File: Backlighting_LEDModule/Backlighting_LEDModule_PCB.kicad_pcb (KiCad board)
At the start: 2 copper layers, 32.2 x 55 mm, 6 parts, among them J1 Conn_02x10_Odd_Even, J11 BOARD_CONN, J2 Conn_02x10_Odd_Even

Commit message: Fix the swapped EFIS filenames and rename the backlight nets to +5V
Two naming defects, no electrical change on any board.

EFIS sheets
-----------
The root sheet pointed EFIS_LEFT at efis_right.kicad_sch and EFIS_RIGHT at
efis_left.kicad_sch. The schematic was correct, since the file behind the
LEFT sheet did hold the L_* signals, but the filenames said the opposite and
anyone reading the files from outside KiCad would have been misled.

The two files are swapped and every reference follows: the sheet properties
in the root schematic and the 49 sheetfile entries the footprints carry on
the board. Each file now matches the sheet that loads it.

  netlist   198 nets, 135 components, not one node moved
  ERC       0 violations
  DRC       6 violations, all cosmetic, 0 unconnected, 0 parity issues

Backlight nets
--------------
Every net in the backlighting chain was called +9V while carrying 5 V, on
all four boards. The white LEDs sit behind 91 Ω: at 5 V that is 21 mA, right
at the rating for a 1206 white LED, while 9 V would put them at 65 mA. The
name was a leftover from an earlier design and was the kind of label that
eventually makes someone connect the wrong supply.

Renamed across Korry_Large, Korry_Small, Backlighting_Dimmer and
Backlighting_LEDModule, in both the schematics and the boards: the power
symbol, its value, which is what actually names the net, and the net entries
on the copper. 88 occurrences. None of those boards had a +5V net already,
so nothing was merged.

Verified against the state committed a moment ago: ERC and DRC counts are
identical on all four boards, before and after, and no board gained or lost
a connection.

The Readme drops these two entries and gains the defects that surfaced while
checking: the Backlighting_Dimmer footprints carry their reference in the
value field instead of the schematic value, so a BOM read from that board is
wrong; its terminal block footprint no longer exists in the KiCad library;
four texts on the Korry_Large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
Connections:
- net +9V renamed +5V
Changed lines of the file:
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@@
 	(net 0 "")
 	(net 1 "GND")
-	(net 2 "+9V")
+	(net 2 "+5V")
 	(footprint "Connector_PinHeader_2.54mm:PinHeader_2x10_P2.54mm_Vertical"
 		(layer "F.Cu")
@@
 			(layers "*.Cu" "*.Mask")
 			(remove_unused_layers no)
-			(net 2 "+9V")
+			(net 2 "+5V")
 			(pinfunction "Pin_2")
 			(pintype "passive")
@@
 			(layers "*.Cu" "*.Mask")
 			(remove_unused_layers no)
-			(net 2 "+9V")
+			(net 2 "+5V")
 			(pinfunction "Pin_4")
 			(pintype "passive")
@@
 			(layers "*.Cu" "*.Mask")
 			(remove_unused_layers no)
-			(net 2 "+9V")
+			(net 2 "+5V")
 			(pinfunction "Pin_6")
 			(pintype "passive")
@@
 			(layers "*.Cu" "*.Mask")
 			(remove_unused_layers no)
-			(net 2 "+9V")
+			(net 2 "+5V")
 			(pinfunction "Pin_8")
 			(pintype "passive")
@@
 			(layers "*.Cu" "*.Mask")
 			(remove_unused_layers no)
-			(net 2 "+9V")
+			(net 2 "+5V")
 			(pinfunction "Pin_10")
 			(pintype "passive")
@@
 			(layers "*.Cu" "*.Mask")
 			(remove_unused_layers no)
-			(net 2 "+9V")
+			(net 2 "+5V")
 			(pinfunction "Pin_12")
 			(pintype "passive")
@@
 			(layers "*.Cu" "*.Mask")
 			(remove_unused_layers no)
-			(net 2 "+9V")
+			(net 2 "+5V")
 			(pinfunction "Pin_14")
 			(pintype "passive")
@@
 			(layers "*.Cu" "*.Mask")
 			(remove_unused_layers no)
-			(net 2 "+9V")
+			(net 2 "+5V")
 			(pinfunction "Pin_16")
 			(pintype "passive")
@@
 			(layers "*.Cu" "*.Mask")
 			(remove_unused_layers no)
-			(net 2 "+9V")
+			(net 2 "+5V")
 			(pinfunction "Pin_18")
 			(pintype "passive")
@@
 			(layers "*.Cu" "*.Mask")
 			(remove_unused_layers no)
-			(net 2 "+9V")
+			(net 2 "+5V")
 			(pinfunction "Pin_20")
 			(pintype "passive")
@@
 			(layers "*.Cu" "*.Mask")
 			(remove_unused_layers no)
-			(net 2 "+9V")
+			(net 2 "+5V")
 			(pinfunction "Pin_2")
 			(pintype "passive")
@@
 			(layers "*.Cu" "*.Mask")
 			(remove_unused_layers no)
-			(net 2 "+9V")
+			(net 2 "+5V")
 			(pinfunction "Pin_4")
 			(pintype "passive")
@@
 			(layers "*.Cu" "*.Mask")
 			(remove_unused_layers no)
-			(net 2 "+9V")
+			(net 2 "+5V")
 			(pinfunction "Pin_6")
 			(pintype "passive")
@@
 			(layers "*.Cu" "*.Mask")
 			(remove_unused_layers no)
-			(net 2 "+9V")
+			(net 2 "+5V")
 			(pinfunction "Pin_8")
 			(pintype "passive")
@@
 			(layers "*.Cu" "*.Mask")
 			(remove_unused_layers no)
-			(net 2 "+9V")
+			(net 2 "+5V")
 			(pinfunction "Pin_10")
 			(pintype "passive")
@@
 			(layers "*.Cu" "*.Mask")
 			(remove_unused_layers no)
-			(net 2 "+9V")
+			(net 2 "+5V")
 			(pinfunction "Pin_12")
 			(pintype "passive")
@@
 			(layers "*.Cu" "*.Mask")
 			(remove_unused_layers no)
-			(net 2 "+9V")
+			(net 2 "+5V")
 			(pinfunction "Pin_14")
 			(pintype "passive")
@@
 			(layers "*.Cu" "*.Mask")
 			(remove_unused_layers no)
-			(net 2 "+9V")
+			(net 2 "+5V")
 			(pinfunction "Pin_16")
 			(pintype "passive")
@@
 			(layers "*.Cu" "*.Mask")
 			(remove_unused_layers no)
-			(net 2 "+9V")
+			(net 2 "+5V")
 			(pinfunction "Pin_18")
 			(pintype "passive")
@@
 			(layers "*.Cu" "*.Mask")
 			(remove_unused_layers no)
-			(net 2 "+9V")
+			(net 2 "+5V")
 			(pinfunction "Pin_20")
 			(pintype "passive")
@@
 			(layers "*.Cu" "*.Mask")
 			(remove_unused_layers no)
-			(net 2 "+9V")
+			(net 2 "+5V")
 			(pinfunction "Pin_2")
 			(pintype "passive")

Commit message: Put +5V on pin 1 of the LEDModule input
Il dimmer ha il +5V sul pin 1 di tutte e tre le sue uscite; il LEDModule ce
l'aveva sul pin 2 del suo ingresso, e su J11 non c'era nessun segno a dirlo.
Da qui il cavetto incrociato: dritto, i LED bianchi si trovano polarizzati
al contrario e non si accendono affatto.

La scheda non ha componenti e ha due soli nodi, N1 (J11 pin 1 piu' le file
dispari) e N2 (J11 pin 2 piu' le pari), quindi il rame non si tocca: bastano
i due nomi di rete e le lettere '+' e '-' che marcano le file. N1 diventa il
+5V marcato '+', e da li' in poi va tutto dritto, dal dimmer fino al Korry.

Aggiunti un '+' e un '-' sopra al contorno di J11, che era nudo ed e' la
ragione per cui ci si sbaglia.

La classe di rete +9V non corrispondeva a nessuna rete; ora e' +5V, cosi'
tutte e due le reti hanno gli 0.8 mm con cui sono gia' disegnate.

Netlist: J11 pin 1 = +5V, file dispari = +5V. ERC e DRC invariati, restano
solo gli avvisi di libreria che c'erano gia'.

Attenzione al montaggio: le schede fatte con questi file vogliono i tre
cavetti dal dimmer DRITTI, non incrociati.

Co-Authored-By: Claude Opus 5 <noreply@anthropic.com>
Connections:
- J1 pad 1: GND -> +5V
- J1 pad 10: +5V -> GND
- J1 pad 11: GND -> +5V
- J1 pad 12: +5V -> GND
- J1 pad 13: GND -> +5V
- J1 pad 14: +5V -> GND
- J1 pad 15: GND -> +5V
- J1 pad 16: +5V -> GND
- J1 pad 17: GND -> +5V
- J1 pad 18: +5V -> GND
- J1 pad 19: GND -> +5V
- J1 pad 2: +5V -> GND
- J1 pad 20: +5V -> GND
- J1 pad 3: GND -> +5V
- J1 pad 4: +5V -> GND
- J1 pad 5: GND -> +5V
- J1 pad 6: +5V -> GND
- J1 pad 7: GND -> +5V
- J1 pad 8: +5V -> GND
- J1 pad 9: GND -> +5V
- J11 pad 1: GND -> +5V
- J11 pad 2: +5V -> GND
- J2 pad 1: GND -> +5V
- J2 pad 10: +5V -> GND
- J2 pad 11: GND -> +5V
- J2 pad 12: +5V -> GND
- J2 pad 13: GND -> +5V
- J2 pad 14: +5V -> GND
- J2 pad 15: GND -> +5V
- J2 pad 16: +5V -> GND
- J2 pad 17: GND -> +5V
- J2 pad 18: +5V -> GND
- J2 pad 19: GND -> +5V
- J2 pad 2: +5V -> GND
- J2 pad 20: +5V -> GND
- J2 pad 3: GND -> +5V
- J2 pad 4: +5V -> GND
- J2 pad 5: GND -> +5V
- J2 pad 6: +5V -> GND
- J2 pad 7: GND -> +5V
- J2 pad 8: +5V -> GND
- J2 pad 9: GND -> +5V
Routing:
- net GND: track 157.8 -> 144.9 mm
- net +5V: track 144.9 -> 157.8 mm

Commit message: Say on the silkscreen what plugs into each connector
Le schede da fabbricate non si leggevano: quasi tutti i valori stavano su
F.Fab, che non va in stampa, e meta' dei connettori aveva come nome il tipo
di morsetto invece di cosa ci va attaccato.

Nessun valore e' stato riscritto: il nome del componente resta quello che
dice KiCad. Si e' lavorato solo sul serigrafico, in due modi.

I valori che gia' dicono qualcosa di utile sono passati su F.Silk, cosi' si
stampano: Backlighting POT sul dimmer, BTN+LED e BK_LED sui Korry, e i 220 e
91 delle due resistenze, che da montare sono due rettangoli identici.

Dove il valore e' il tipo di morsetto e stampalo non servirebbe a niente, il
valore resta dov'e' e accanto ci va una scritta che dice dove va il filo:

  PSU        J1 -> 9V IN, J2/J3/J4 -> 5V BACKLIGHT, J5 -> 5V MAINBOARD
  Dimmer     J32 -> 5V IN, J12/J13/J14 -> TO LEDMODULE
  LEDModule  J11 -> 5V IN

Ogni posizione e' stata verificata contro pad, altre scritte, contorni
serigrafici e bordo scheda, e poi ricontrollata col DRC, che e' l'unico a
sapere quanto e' larga davvero l'apertura di maschera di un foro di
fissaggio: la scritta di J14 ci finiva sopra, e il valore di J1 sul Korry
grande finiva a cavallo del bordo.

Tutte e cinque le schede: 0 scollegamenti, 0 differenze con lo schema,
nessuna violazione serigrafica. Restano solo gli avvisi di libreria.

Co-Authored-By: Claude Opus 5 <noreply@anthropic.com>
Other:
- board text added: "5V IN"
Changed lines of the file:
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@@
+		)
+	)
+	(gr_text "5V IN"
+		(at 117.8 94 0)
+		(layer "F.SilkS")
+		(effects
+			(font
+				(size 1 1)
+				(thickness 0.15)
+			)
 		)
 	)

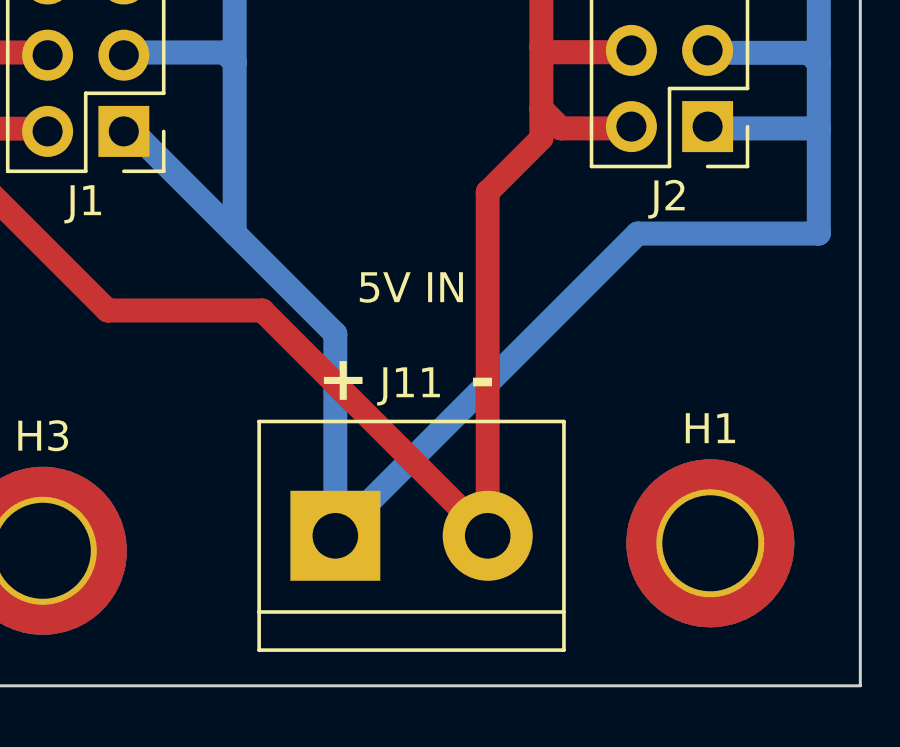
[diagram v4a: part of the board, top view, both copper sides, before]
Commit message: Use the same terminal block everywhere
Le due schede backlighting stavano su TerminalBlock_bornier-2_P5.08mm, che
la libreria KiCad 10 non ha piu'. Il morsetto e' lo stesso che sta su PSU e
mainboard, quindi ora lo e' anche nei file: Phoenix PT-1,5-2-5.0-H, su
J12, J13, J14 e J32 del dimmer e su J11 del LEDModule.

Cosa cambia nel rame: passo 5.08 -> 5.00, pad 3.0 -> 2.6, foro 1.52 -> 1.30.
Gli 8 centesimi di passo non li sente nessuno; il foro piu' stretto e' la
misura giusta per quel morsetto.

Il corpo Phoenix e' pero' 1.64 mm piu' profondo del bornier, e questo si
sente:
 - J12, J13 e J14 arrivavano a 0.04 mm dal courtyard dei fori di fissaggio.
   Alzati di un decimo;
 - J32 e J11 stavano a filo del bordo scheda col vecchio corpo e col nuovo
   sporgevano. Rientrati, J11 esattamente dove stava prima la sua faccia
   esterna;
 - le estremita' delle piste sono state riagganciate ai nuovi centri dei
   pad, 13 in tutto, invece di lasciarle fuori centro;
 - le tre scritte TO LEDMODULE non ci stavano piu' sopra ai morsetti: una
   sola sotto alla fila, che sono tre uscite identiche.

Resta un solo avviso sul dimmer, ed e' geometria, non una svista: il
disegno dell'imbocco filo di J32 sfiora il bordo scheda a 0.02 mm. Per
rientrare J32 dovrebbe scendere, ma sotto ha C4 a 0.04 mm dal suo
courtyard: la finestra utile e' alta 10.49 mm per un corpo da 10. Tenuto
l'errore di courtyard risolto e lasciato l'avviso serigrafico, che vuol dire
solo che un pezzetto di inchiostro viene tagliato al bordo.

I problemi noti sono ora vuoti. Le zone delle due schede sono da riempire.

Co-Authored-By: Claude Opus 5 <noreply@anthropic.com>
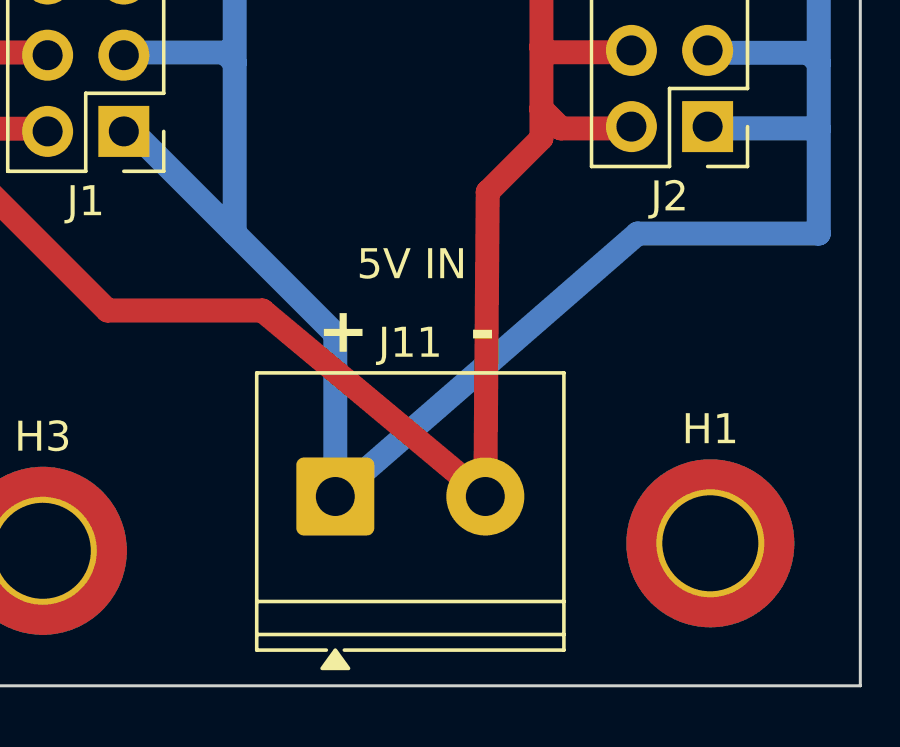
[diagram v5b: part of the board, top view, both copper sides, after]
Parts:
- J11: footprint TerminalBlock:TerminalBlock_bornier-2_P5.08mm -> TerminalBlock_Phoenix:TerminalBlock_Phoenix_PT-1,5-2-5.0-H_1x02_P5.00mm_Horizontal
- moved J11 1.31 mm to (115.2, 100.9)
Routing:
- net GND: track 144.9 -> 142.7 mm
- net +5V: track 157.8 -> 155.6 mm
